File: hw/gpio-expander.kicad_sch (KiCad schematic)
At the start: 18 parts, among them U2001 MCP23S17, U2002 SN74LVC2G14DBV, U2003 SN74LVC2G14DBV, U2004 SN74LVC2G14DBV, U2005 SN74LVC2G14DBV, U2006 SN74LVC2G14DBV, U2007 SN74LVC2G14DBV, U2008 SN74LVC2G14DBV, U2009 SN74LVC2G14DBV

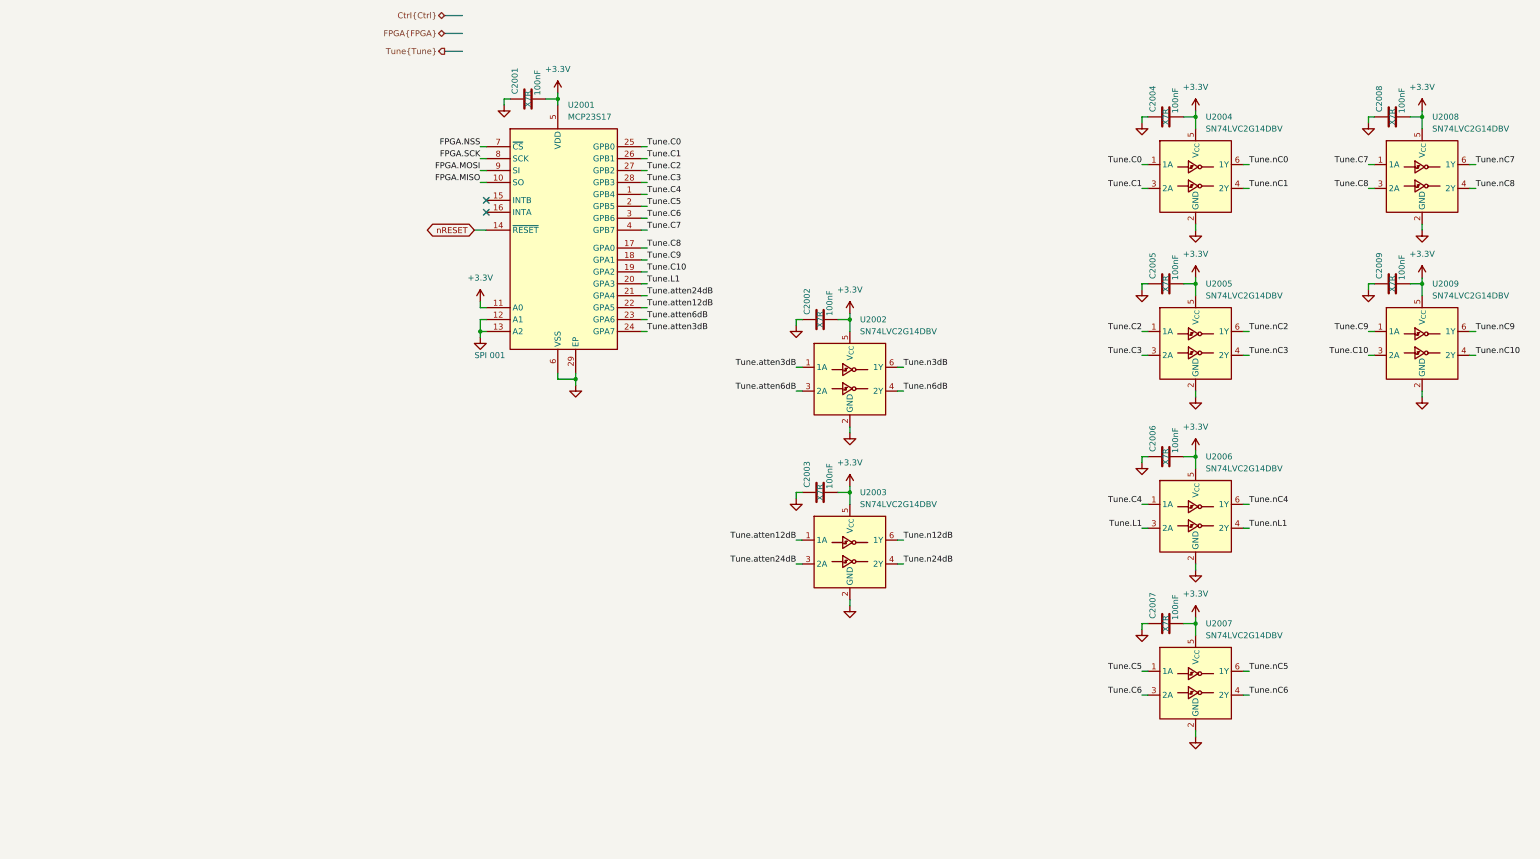
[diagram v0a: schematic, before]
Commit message: Added RC filter for "static" signals to avoid coupling noise from 3.3V logic into signal path.
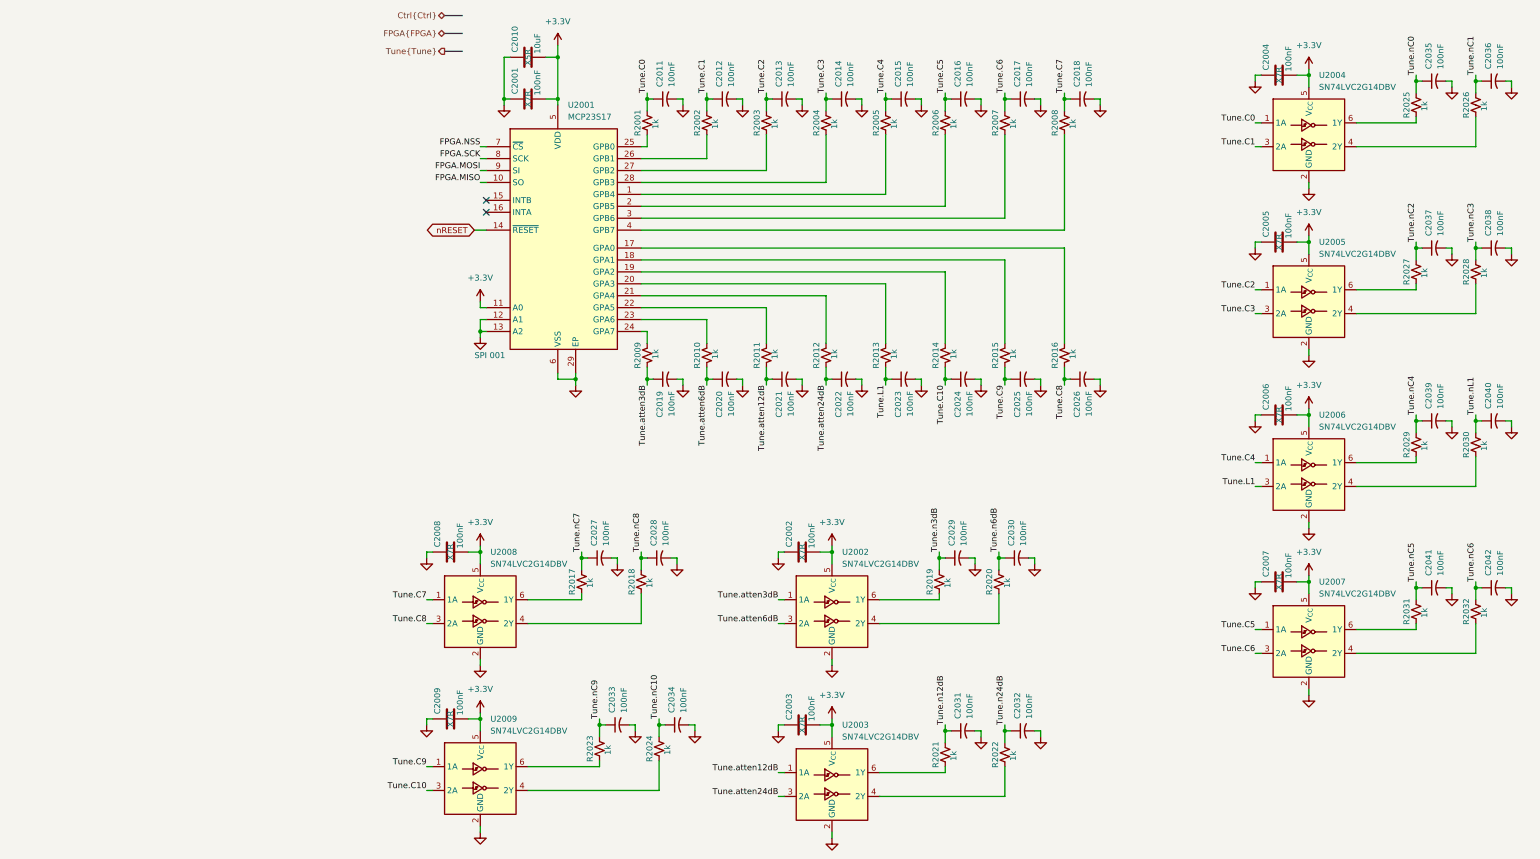
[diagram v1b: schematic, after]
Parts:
- added C2010: 10uF, Capacitor_SMD:C_0603_1608Metric, symbol Device:C
- added C2011, C2012, C2013, C2014, C2015, C2016, C2017, C2018, C2019, C2020, C2021, C2022, C2023, C2024, C2025, C2026, C2027, C2028, C2029, C2030, C2031, C2032, C2033, C2034, C2035, C2036, C2037, C2038, C2039, C2040, C2041, C2042: 100nF, Capacitor_SMD:C_0402_1005Metric, symbol Device:C_Small_US
- added R2001, R2002, R2003, R2004, R2005, R2006, R2007, R2008, R2009, R2010, R2011, R2012, R2013, R2014, R2015, R2016, R2017, R2018, R2019, R2020, R2021, R2022, R2023, R2024, R2025, R2026, R2027, R2028, R2029, R2030, R2031, R2032: 1k, Resistor_SMD:R_0402_1005Metric, symbol Device:R_Small_US
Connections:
- net +3.3V: now also C2010.2
- net GND: now also C2010.1, C2011.2, C2012.2, C2013.2, C2014.2, C2015.2, C2016.2, C2017.2, C2018.2, C2019.2, C2020.2, C2021.2, C2022.2, C2023.2, C2024.2, C2025.2, C2026.2, C2027.2, C2028.2, C2029.2, C2030.2, C2031.2, C2032.2, C2033.2, C2034.2, C2035.2, C2036.2, C2037.2, C2038.2, C2039.2, C2040.2, C2041.2, C2042.2
- net Tune.C0: now also C2011.1, R2001.2; no longer U2001.25 (GPB0)
- net Tune.C1: now also C2012.1, R2002.2; no longer U2001.26 (GPB1)
- net Tune.C10: now also C2024.1, R2014.2; no longer U2001.19 (GPA2)
- net Tune.C2: now also C2013.1, R2003.2; no longer U2001.27 (GPB2)
- net Tune.C3: now also C2014.1, R2004.2; no longer U2001.28 (GPB3)
- net Tune.C4: now also C2015.1, R2005.2; no longer U2001.1 (GPB4)
- net Tune.C5: now also C2016.1, R2006.2; no longer U2001.2 (GPB5)
- net Tune.C6: now also C2017.1, R2007.2; no longer U2001.3 (GPB6)
- net Tune.C7: now also C2018.1, R2008.2; no longer U2001.4 (GPB7)
- net Tune.C8: now also C2026.1, R2016.2; no longer U2001.17 (GPA0)
- net Tune.C9: now also C2025.1, R2015.2; no longer U2001.18 (GPA1)
- net Tune.L1: now also C2023.1, R2013.2; no longer U2001.20 (GPA3)
- net Tune.atten12dB: now also C2021.1, R2011.2; no longer U2001.22 (GPA5)
- net Tune.atten24dB: now also C2022.1, R2012.2; no longer U2001.21 (GPA4)
- net Tune.atten3dB: now also C2019.1, R2009.2; no longer U2001.24 (GPA7)
- net Tune.atten6dB: now also C2020.1, R2010.2; no longer U2001.23 (GPA6)
- net Tune.n12dB: now also C2031.1, R2021.2; no longer U2003.6 (1Y)
- net Tune.n24dB: now also C2032.1, R2022.2; no longer U2003.4 (2Y)
- net Tune.n3dB: now also C2029.1, R2019.2; no longer U2002.6 (1Y)
- net Tune.n6dB: now also C2030.1, R2020.2; no longer U2002.4 (2Y)
- net Tune.nC0: now also C2035.1, R2025.2; no longer U2004.6 (1Y)
- net Tune.nC1: now also C2036.1, R2026.2; no longer U2004.4 (2Y)
- net Tune.nC10: now also C2034.1, R2024.2; no longer U2009.4 (2Y)
- net Tune.nC2: now also C2037.1, R2027.2; no longer U2005.6 (1Y)
- net Tune.nC3: now also C2038.1, R2028.2; no longer U2005.4 (2Y)
- net Tune.nC4: now also C2039.1, R2029.2; no longer U2006.6 (1Y)
- net Tune.nC5: now also C2041.1, R2031.2; no longer U2007.6 (1Y)
- net Tune.nC6: now also C2042.1, R2032.2; no longer U2007.4 (2Y)
- net Tune.nC7: now also C2027.1, R2017.2; no longer U2008.6 (1Y)
- net Tune.nC8: now also C2028.1, R2018.2; no longer U2008.4 (2Y)
- net Tune.nC9: now also C2033.1, R2023.2; no longer U2009.6 (1Y)
- net Tune.nL1: now also C2040.1, R2030.2; no longer U2006.4 (2Y)
- new net: R2012.1, U2001.21 (GPA4)
- new net: R2014.1, U2001.19 (GPA2)
- new net: R2016.1, U2001.17 (GPA0)
- new net: R2032.1, U2007.4 (2Y)
- new net: R2031.1, U2007.6 (1Y)
- new net: R2025.1, U2004.6 (1Y)
- new net: R2011.1, U2001.22 (GPA5)
- new net: R2020.1, U2002.4 (2Y)
- new net: R2009.1, U2001.24 (GPA7)
- new net: R2010.1, U2001.23 (GPA6)
- new net: R2023.1, U2009.6 (1Y)
- new net: R2019.1, U2002.6 (1Y)
- new net: R2018.1, U2008.4 (2Y)
- new net: R2004.1, U2001.28 (GPB3)
- new net: R2002.1, U2001.26 (GPB1)
- new net: R2015.1, U2001.18 (GPA1)
- new net: R2006.1, U2001.2 (GPB5)
- new net: R2007.1, U2001.3 (GPB6)
- new net: R2005.1, U2001.1 (GPB4)
- new net: R2013.1, U2001.20 (GPA3)
- new net: R2001.1, U2001.25 (GPB0)
- new net: R2003.1, U2001.27 (GPB2)
- new net: R2008.1, U2001.4 (GPB7)
- new net: R2030.1, U2006.4 (2Y)
- new net: R2028.1, U2005.4 (2Y)
- new net: R2027.1, U2005.6 (1Y)
- new net: R2017.1, U2008.6 (1Y)
- new net: R2029.1, U2006.6 (1Y)
- new net: R2021.1, U2003.6 (1Y)
- new net: R2026.1, U2004.4 (2Y)
- new net: R2022.1, U2003.4 (2Y)
- new net: R2024.1, U2009.4 (2Y)
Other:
- moved on the sheet: C2002, C2003, C2004, C2005, C2006, C2007, C2008, C2009, U2002, U2003, U2004, U2005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

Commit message: Checkpoint reverting away from VLF extension
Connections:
- net Tune.C0: no longer U2004.1 (1A)
- net Tune.C1: no longer U2004.3 (2A)
- net Tune.C10: no longer U2009.3 (2A)
- net Tune.C2: no longer U2005.1 (1A)
- net Tune.C3: no longer U2005.3 (2A)
- net Tune.C4: no longer U2006.1 (1A)
- net Tune.C5: no longer U2007.1 (1A)
- net Tune.C6: no longer U2007.3 (2A)
- net Tune.C7: no longer U2008.1 (1A)
- net Tune.C8: no longer U2008.3 (2A)
- net Tune.C9: no longer U2009.1 (1A)
- net Tune.L1: no longer U2006.3 (2A)
- net Tune.atten12dB: no longer U2003.1 (1A)
- net Tune.atten24dB: no longer U2003.3 (2A)
- net Tune.atten3dB: no longer U2002.1 (1A)
- net Tune.atten6dB: no longer U2002.3 (2A)
- net db24: now reaches R2012.1, U2001.21 (GPA4)
- net db24: now also U2003.3 (2A)
- net C10: now reaches R2014.1, U2001.19 (GPA2)
- net C10: now also U2009.3 (2A)
- net C8: now reaches R2016.1, U2001.17 (GPA0)
- net C8: now also U2008.3 (2A)
- net db12: now reaches R2011.1, U2001.22 (GPA5)
- net db12: now also U2003.1 (1A)
- net db3: now reaches R2009.1, U2001.24 (GPA7)
- net db3: now also U2002.1 (1A)
- net db6: now reaches R2010.1, U2001.23 (GPA6)
- net db6: now also U2002.3 (2A)
- net C3: now reaches R2004.1, U2001.28 (GPB3)
- net C3: now also U2005.3 (2A)
- net C1: now reaches R2002.1, U2001.26 (GPB1)
- net C1: now also U2004.3 (2A)
- net C9: now reaches R2015.1, U2001.18 (GPA1)
- net C9: now also U2009.1 (1A)
- net C5: now reaches R2006.1, U2001.2 (GPB5)
- net C5: now also U2007.1 (1A)
- net C6: now reaches R2007.1, U2001.3 (GPB6)
- net C6: now also U2007.3 (2A)
- net C4: now reaches R2005.1, U2001.1 (GPB4)
- net C4: now also U2006.1 (1A)
- net L1: now reaches R2013.1, U2001.20 (GPA3)
- net L1: now also U2006.3 (2A)
- net C0: now reaches R2001.1, U2001.25 (GPB0)
- net C0: now also U2004.1 (1A)
- net C2: now reaches R2003.1, U2001.27 (GPB2)
- net C2: now also U2005.1 (1A)
- net C7: now reaches R2008.1, U2001.4 (GPB7)
- net C7: now also U2008.1 (1A)

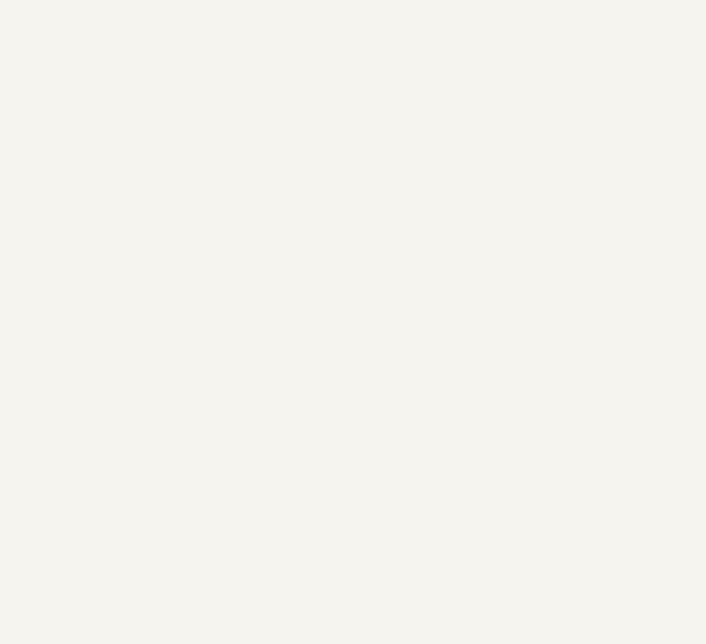
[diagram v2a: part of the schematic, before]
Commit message: Possibly preparing to use GreenPAK for AS183-92LF control signals via I2C?
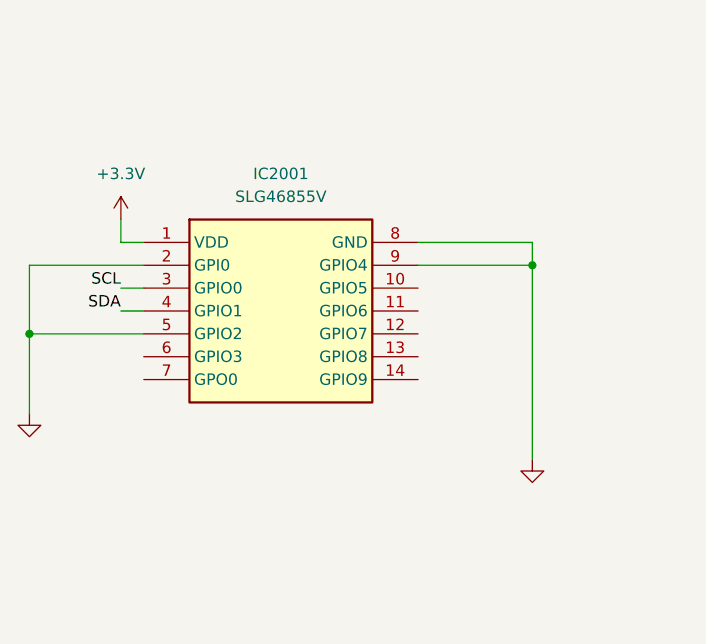
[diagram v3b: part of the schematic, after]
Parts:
- added IC2001: SLG46855V, SLG46855V, symbol Library:SLG46855V
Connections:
- net +3.3V: now also IC2001.1 (VDD)
- net GND: now also IC2001.2 (GPI0), IC2001.5 (GPIO2), IC2001.8 (GND), IC2001.9 (GPIO4)
- new net SCL: IC2001.3 (GPIO0)
- new net SDA: IC2001.4 (GPIO1)

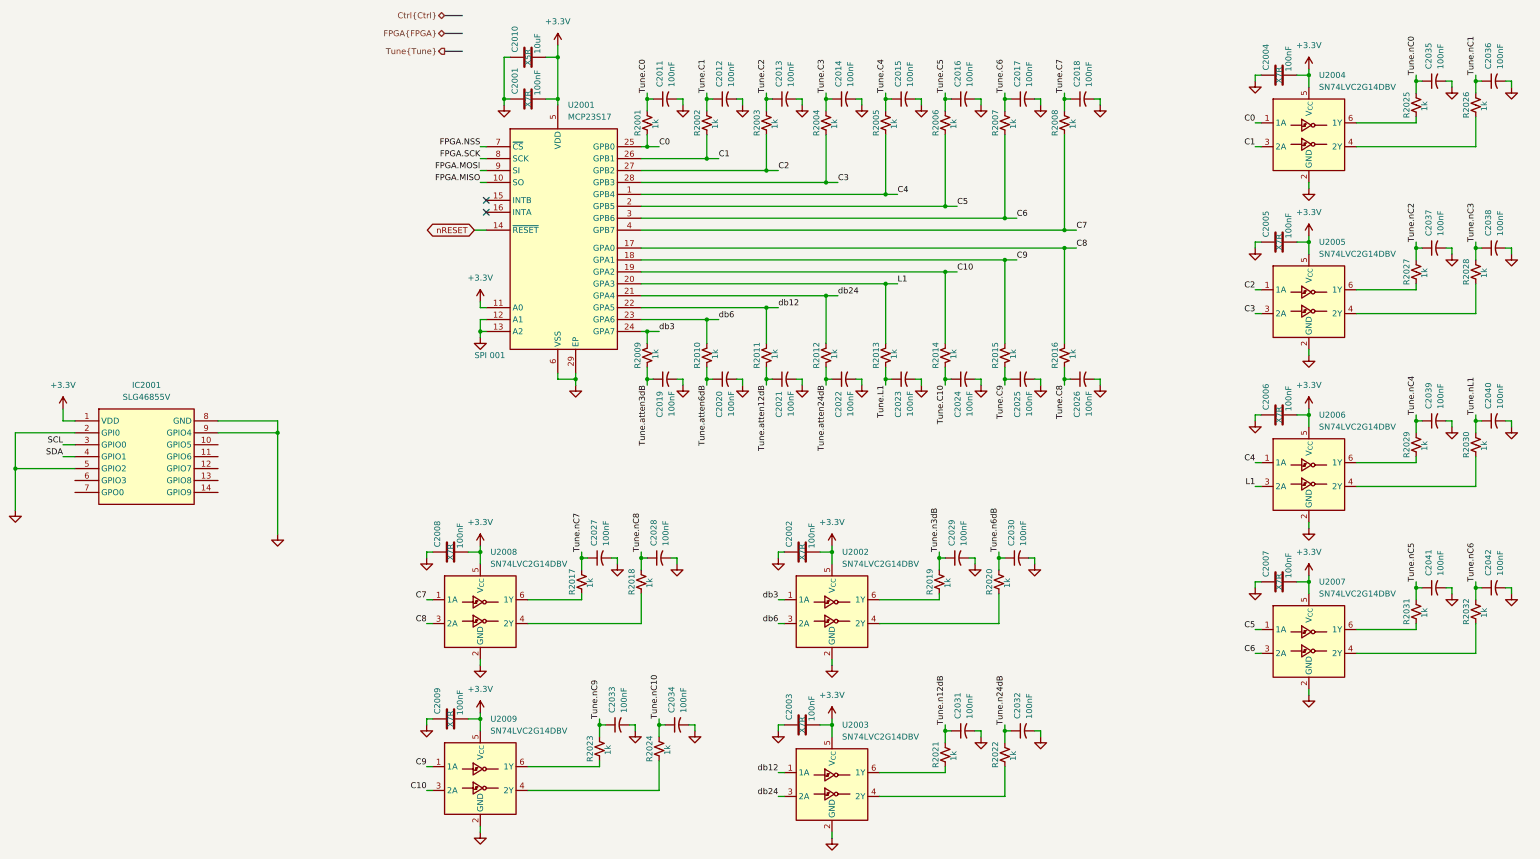
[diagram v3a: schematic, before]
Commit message: Now using STM32C011 for the GPIO expanders and it is WAY better routing and placing and event cost
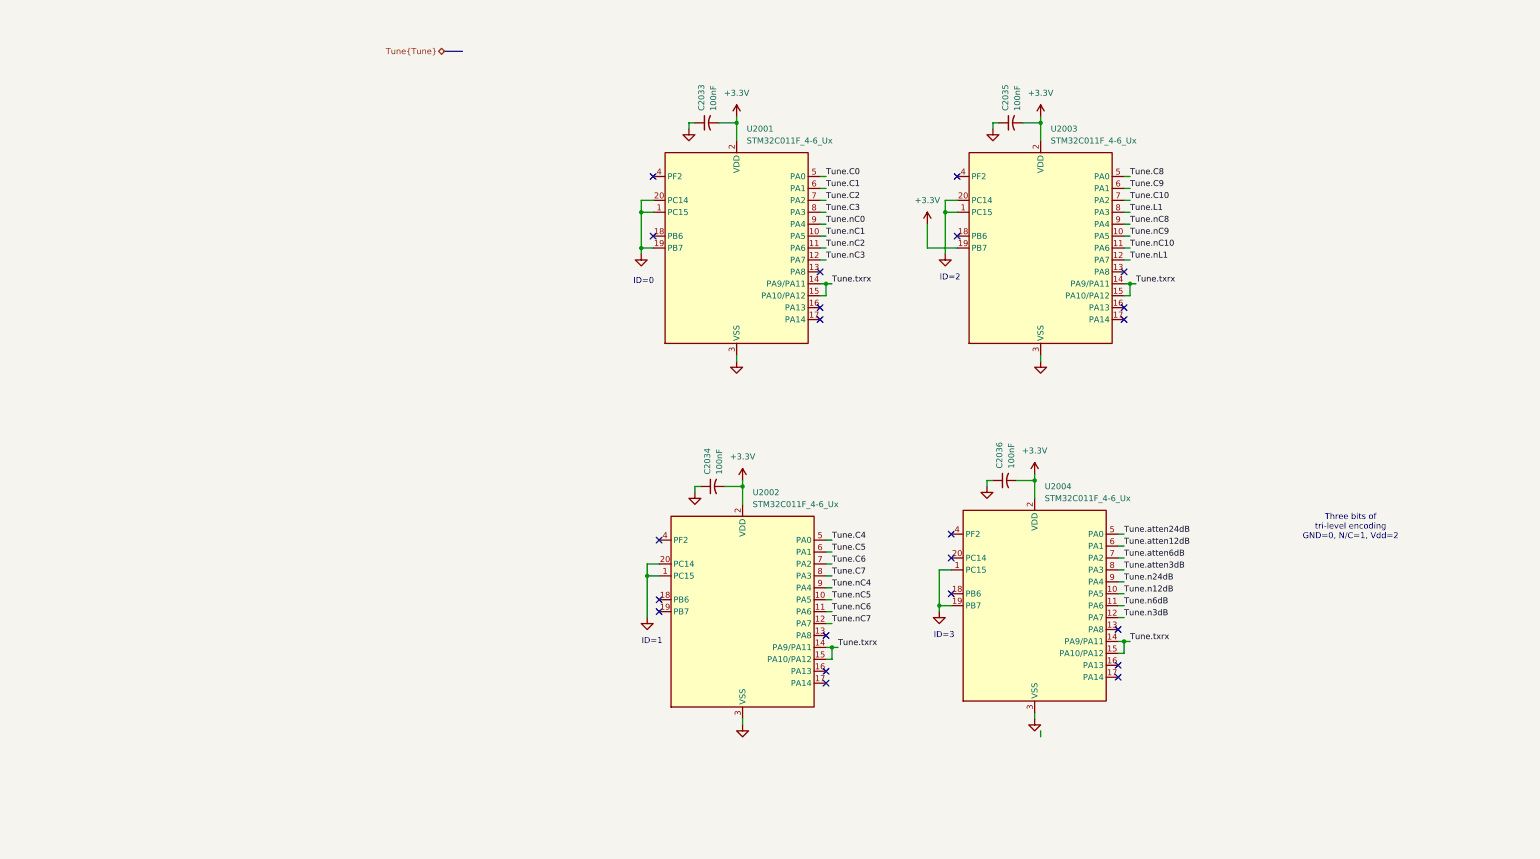
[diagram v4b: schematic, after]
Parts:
- removed C2001, C2002, C2003, C2004, C2005, C2006, C2007, C2008, C2009: 100nF, Capacitor_SMD:C_0603_1608Metric, symbol Device:C
- removed C2010: 10uF, Capacitor_SMD:C_0603_1608Metric, symbol Device:C
- removed C2011, C2012, C2013, C2014, C2015, C2016, C2017, C2018, C2019, C2020, C2021, C2022, C2023, C2024, C2025, C2026, C2027, C2028, C2029, C2030, C2031, C2032, C2037, C2038, C2039, C2040, C2041, C2042: 100nF, Capacitor_SMD:C_0402_1005Metric, symbol Device:C_Small_US
- removed IC2001: SLG46855V, SLG46855V, symbol Library:SLG46855V
- removed R2001, R2002, R2003, R2004, R2005, R2006, R2007, R2008, R2009, R2010, R2011, R2012, R2013, R2014, R2015, R2016, R2017, R2018, R2019, R2020, R2021, R2022, R2023, R2024, R2025, R2026, R2027, R2028, R2029, R2030, R2031, R2032: 1k, Resistor_SMD:R_0402_1005Metric, symbol Device:R_Small_US
- removed U2001: MCP23S17, QFN65P600X600X100-29N-D, symbol Library:MCP23S17T-E_ML
- removed U2002, U2003, U2004, U2005, U2006, U2007, U2008, U2009: SN74LVC2G14DBV, Package_TO_SOT_SMD:SOT-23-6, symbol 74xGxx:SN74LVC2G14DBV
- added U2001, U2002, U2003, U2004: STM32C011F_4-6_Ux, Library:QFN50P300X300X60-20N-D, symbol MCU_ST_STM32C0:STM32C011F_4-6_Ux
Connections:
- net +3.3V: now also C2033.2, C2034.2, C2035.2, C2036.2, U2001.2 (VDD), U2002.2 (VDD), U2003.19 (PB7), U2003.2 (VDD), U2004.2 (VDD)
- net GND: now also C2033.1, C2034.1, C2035.1, C2036.1, U2001.1 (PC15), U2001.19 (PB7), U2001.20 (PC14), U2001.3 (VSS), U2002.1 (PC15), U2002.20 (PC14), U2002.3 (VSS), U2003.1 (PC15), U2003.20 (PC14), U2003.3 (VSS), U2004.1 (PC15), U2004.19 (PB7), U2004.3 (VSS); no longer C2033.2, C2034.2, C2035.2, C2036.2
- net Tune.C0: now also U2001.5 (PA0)
- net Tune.C1: now also U2001.6 (PA1)
- net Tune.C10: now also U2003.7 (PA2)
- net Tune.C2: now also U2001.7 (PA2)
- net Tune.C3: now also U2001.8 (PA3)
- net Tune.C4: now also U2002.5 (PA0)
- net Tune.C5: now also U2002.6 (PA1)
- net Tune.C6: now also U2002.7 (PA2)
- net Tune.C7: now also U2002.8 (PA3)
- net Tune.C8: now also U2003.5 (PA0)
- net Tune.C9: now also U2003.6 (PA1)
- net Tune.L1: now also U2003.8 (PA3)
- net Tune.atten12dB: now also U2004.6 (PA1)
- net Tune.atten24dB: now also U2004.5 (PA0)
- net Tune.atten3dB: now also U2004.8 (PA3)
- net Tune.atten6dB: now also U2004.7 (PA2)
- net Tune.n12dB: now also U2004.10 (PA5)
- net Tune.n24dB: now also U2004.9 (PA4)
- net Tune.n3dB: now also U2004.12 (PA7)
- net Tune.n6dB: now also U2004.11 (PA6)
- net Tune.nC0: now also U2001.9 (PA4); no longer C2035.1
- net Tune.nC1: now also U2001.10 (PA5); no longer C2036.1
- net Tune.nC10: now also U2003.11 (PA6); no longer C2034.1
- net Tune.nC2: now also U2001.11 (PA6)
- net Tune.nC3: now also U2001.12 (PA7)
- net Tune.nC4: now also U2002.9 (PA4)
- net Tune.nC5: now also U2002.10 (PA5)
- net Tune.nC6: now also U2002.11 (PA6)
- net Tune.nC7: now also U2002.12 (PA7)
- net Tune.nC8: now also U2003.9 (PA4)
- net Tune.nC9: now also U2003.10 (PA5); no longer C2033.1
- net Tune.nL1: now also U2003.12 (PA7)
- new net Tune.txrx: U2001.14 (PA9/PA11), U2001.15 (PA10/PA12), U2002.14 (PA9/PA11), U2002.15 (PA10/PA12), U2003.14 (PA9/PA11), U2003.15 (PA10/PA12), U2004.14 (PA9/PA11), U2004.15 (PA10/PA12)
- no-connect marks 2 -> 22
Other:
- note added: "ID=0"
- note added: "ID=1"
- note added: "ID=2"
- note added: "ID=3"
- note added: "Three bits of tri-level encoding GND=0, N/C=1, Vdd=2"
- note removed: "SPI 001"
